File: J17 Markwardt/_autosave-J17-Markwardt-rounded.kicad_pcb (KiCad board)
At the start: 2 copper layers, 16.5 x 28.8 mm, 6 parts, among them J1 USB_C_Receptacle_USB2.0, J2 829-22-005-20-001101

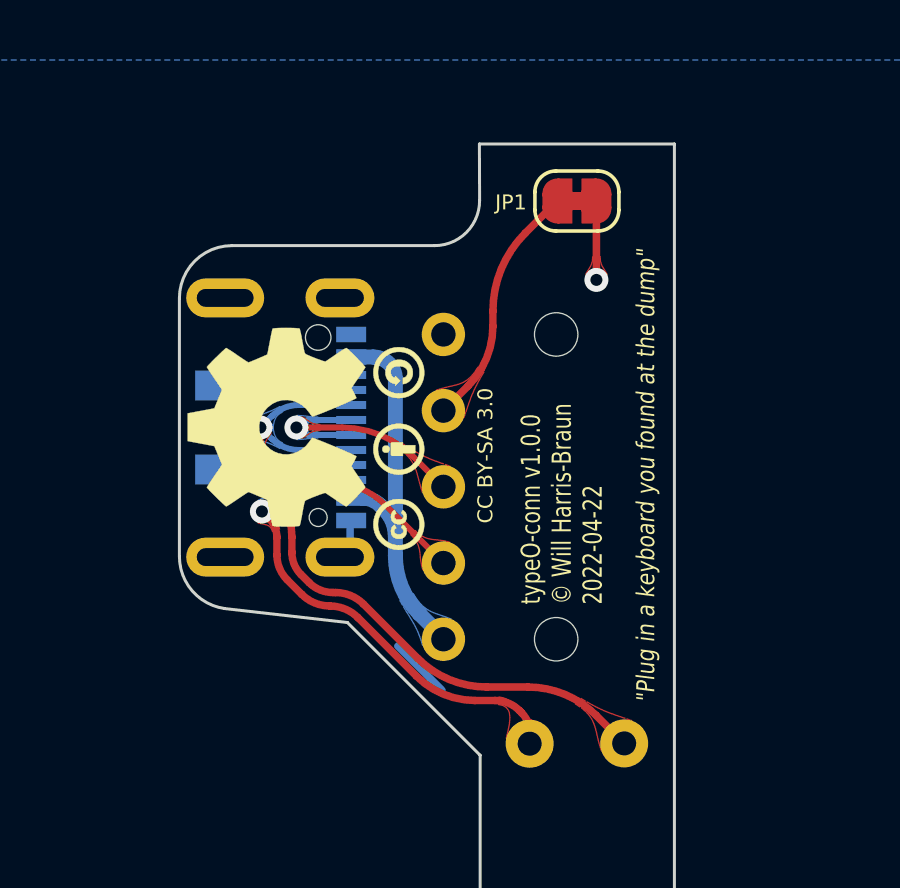
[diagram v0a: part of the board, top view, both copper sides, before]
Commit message: Rename connector to J17 Markwardt
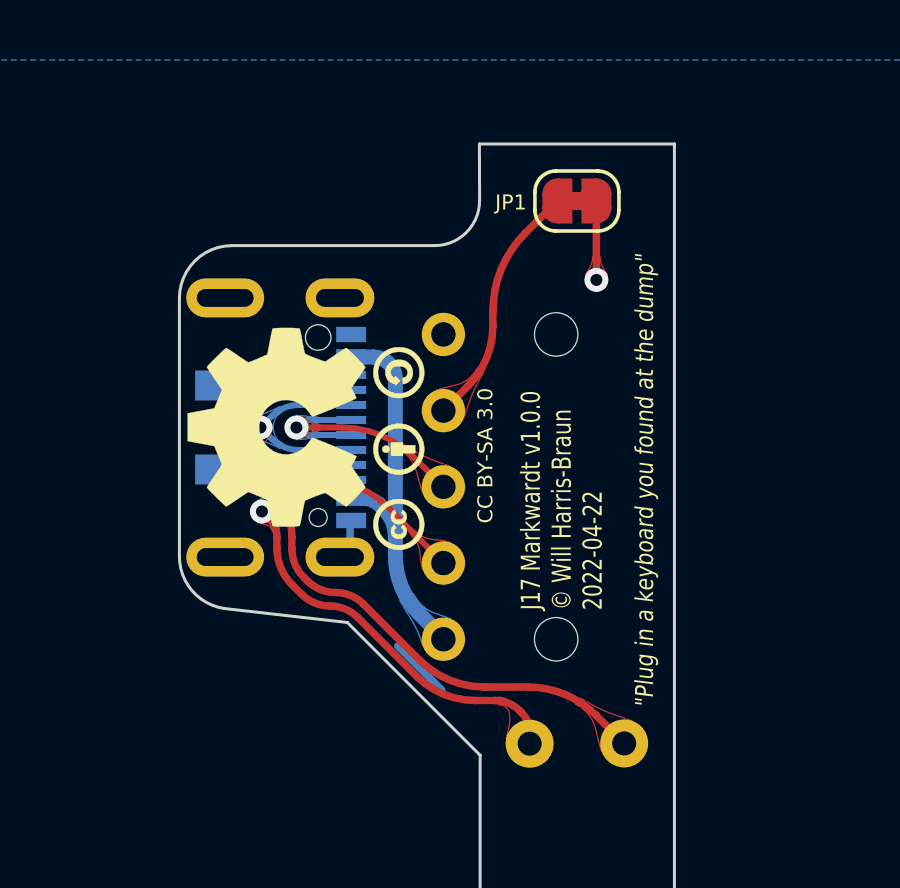
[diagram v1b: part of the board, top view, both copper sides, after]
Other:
- board text added: "J17 Markwardt v1.0.0 © Will Harris-Braun 2022-04-22"
- board text removed: "typeO-conn v1.0.0 © Will Harris-Braun 2022-04-22"
